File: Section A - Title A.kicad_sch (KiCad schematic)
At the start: 2 parts, among them U1 ME54BS13_V1.0

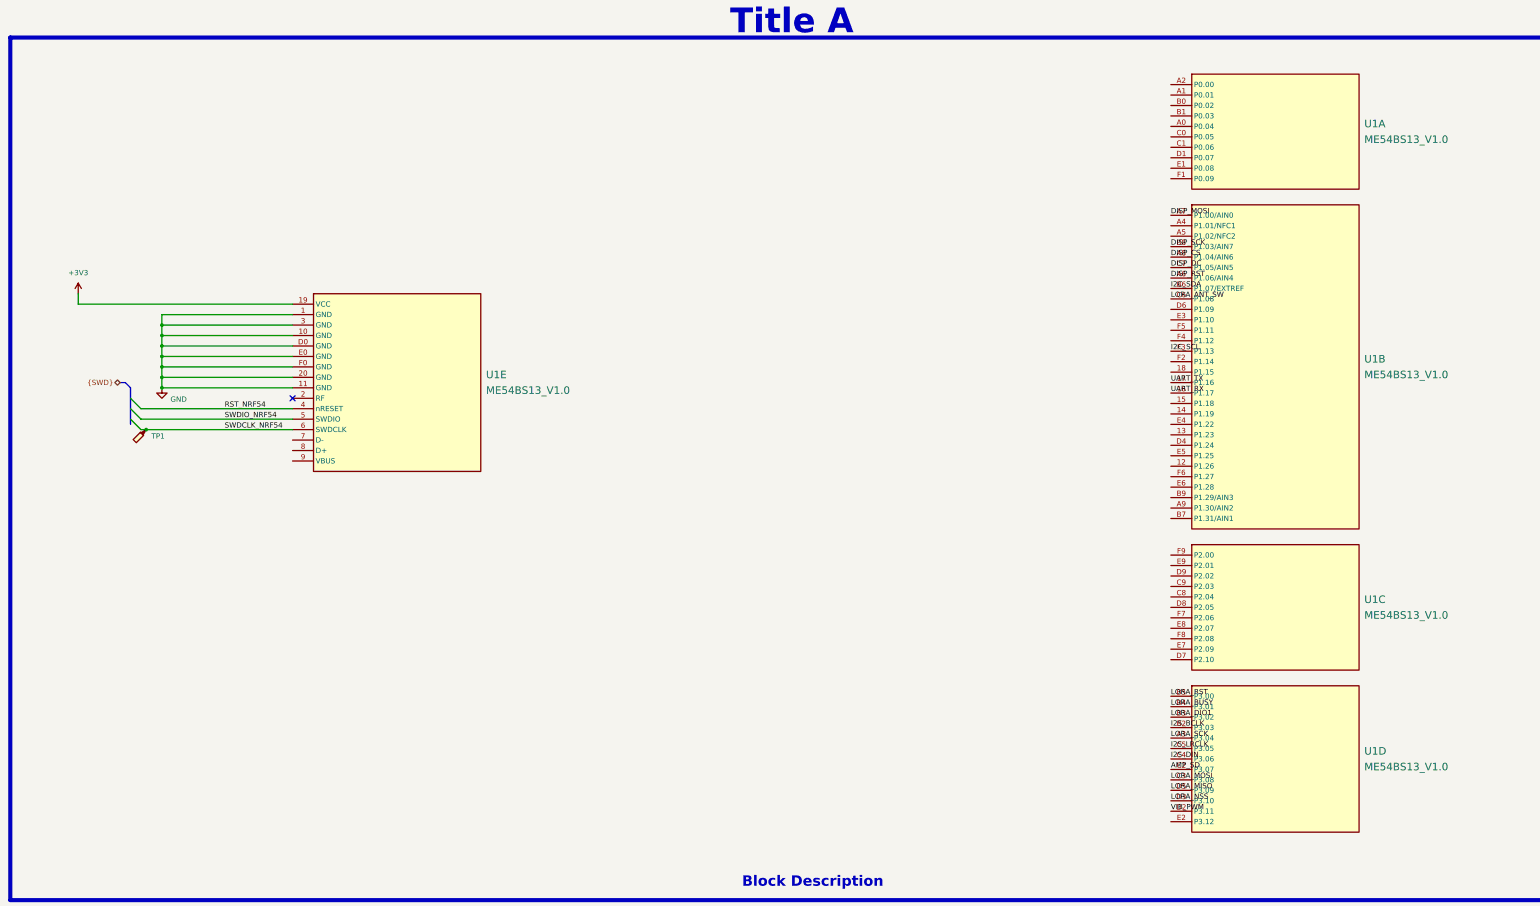
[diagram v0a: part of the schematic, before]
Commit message: Add power supply, connectors, LoRa, gas sensor, audio, and display sheets
Adds nPM1300 power management, USB-C connectors, Minew LoRa module,
multi-gas sensing (CO2/particulate), audio, and display schematics
along with the supporting component libraries and updated PCB routing.

Co-Authored-By: Claude Sonnet 5 <noreply@anthropic.com>
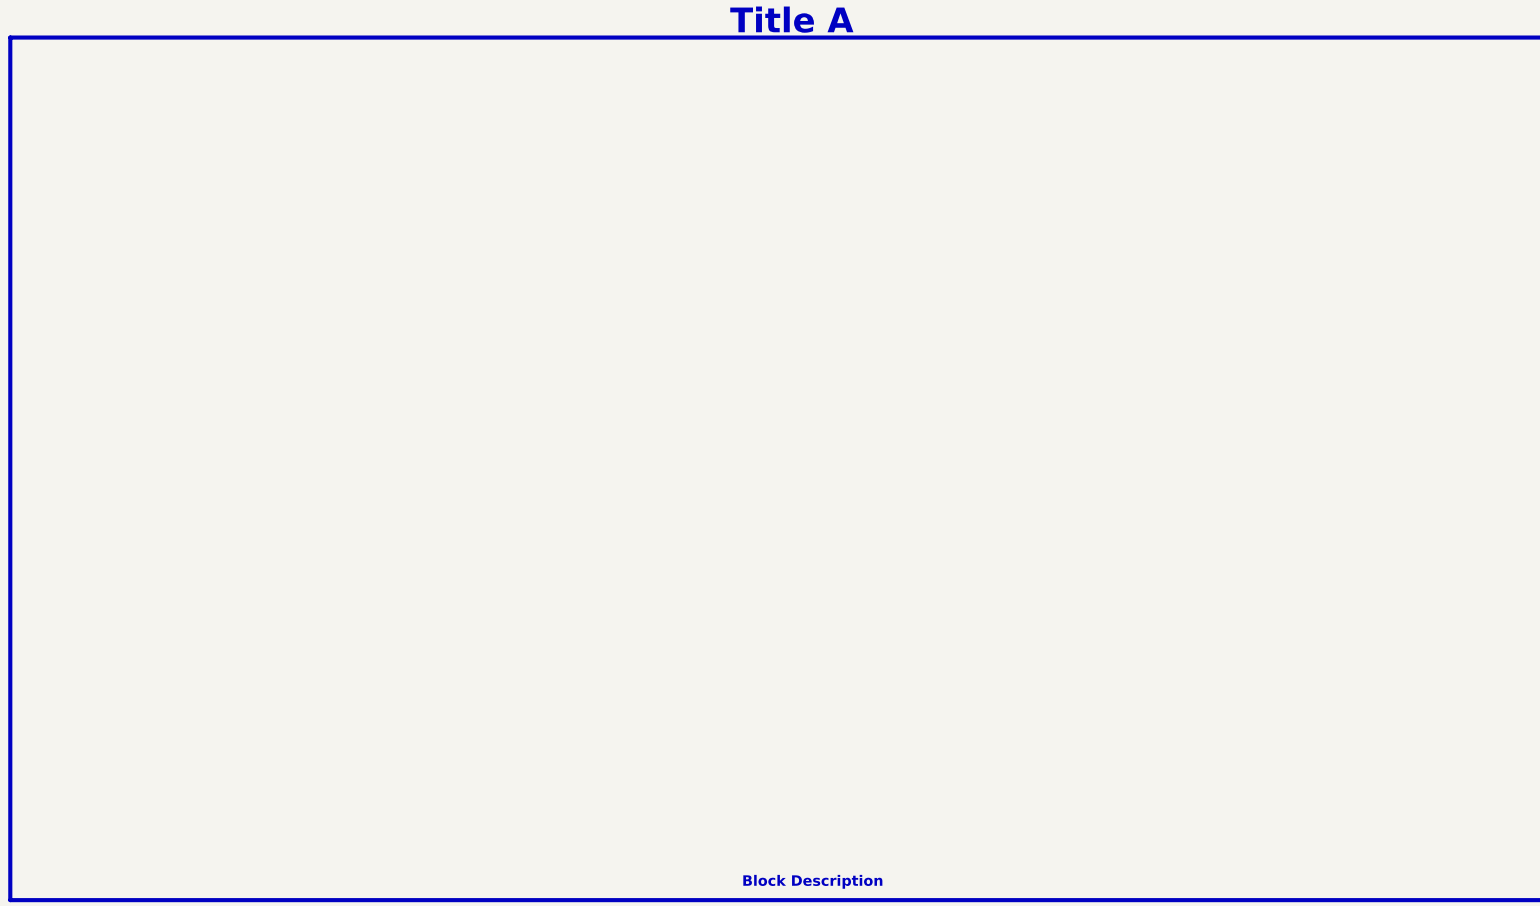
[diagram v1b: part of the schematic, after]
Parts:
- removed TP1: TestPoint_Probe, TestPoint:TestPoint_Pad_D1.0mm, symbol Connector:TestPoint_Probe
- removed U1: ME54BS13_V1.0, ME54BS13_V1.0, symbol minew:ME54BS13_V1.0
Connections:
- no-connect marks 1 -> 0
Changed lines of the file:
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@@
+(kicad_sch
+	(version 20250114)
+	(generator "eeschema")
+	(generator_version "9.0")
+	(paper "A3")
+	(title_block
+		(title "Sheet Title A")
+		(date "2025-01-12")
+		(rev "${REVISION}")
+		(company "${COMPANY}")
+	)
+	(rectangle
+		(start 15.24 30.48)
+		(end 405.13 240.03)
+		(stroke
+			(width 1)
+			(type default)
+			(color 200 200 200 1)
+		)
+		(fill
+			(type none)
+		)
+	)
+	(text "J. Pieper ADC investigation"
+		(exclude_from_sim no)
+		(at 265.938 258.318 0)
+		(effects
+			(font
+				(face "Arial")
+				(size 1.27 1.27)
+				(color 0 0 0 1)
+			)
+			(justify left bottom)
+			(href "https://jpieper.com/2023/07/24/stm32g4-adc-performance-part-2/")
+		)
+	)
+	(text "STM32G474 Datasheet p.81"
+		(exclude_from_sim no)
+		(at 265.938 254.508 0)
+		(effects
+			(font
+				(face "Arial")
+				(size 1.27 1.27)
+				(color 0 0 0 1)
+			)
+			(justify left bottom)
+			(href "https://www.st.com/resource/en/datasheet/stm32g474cb.pdf")
+		)
+	)
+	(text "AN5346"
+		(exclude_from_sim no)
+		(at 265.938 250.698 0)
+		(effects
+			(font
+				(face "Arial")
+				(size 1.27 1.27)
+				(color 0 0 0 1)
+			)
+			(justify left bottom)
+			(href "https://www.st.com/resource/en/application_note/an5346-stm32g4-adc-use-tips-and-recommendations-stmicroelectronics.pdf")
+		)
+	)
+	(text_box "[${#}] ${TITLE}"
+		(exclude_from_sim no)
+		(at 168.91 15.24 0)
+		(size 72.39 12.7)
+		(margins 4.4999 4.4999 4.4999 4.4999)
+		(stroke
+			(width -0.0001)
+			(type default)
+		)
+		(fill
+			(type none)
+		)
+		(effects
+			(font
+				(face "Times New Roman")
+				(size 6 6)
+				(thickness 1.2)
+				(bold yes)
+				(color 162 22 34 1)
+			)
+		)
+	)
+	(text_box "Block Description"
+		(exclude_from_sim no)
+		(at 16.51 231.14 0)
+		(size 387.35 7.62)
+		(margins 1.9049 1.9049 1.9049 1.9049)
+		(stroke
+			(width -0.0001)
+			(type default)
+		)
+		(fill
+			(type none)
+		)
+		(effects
+			(font
+				(face "Times New Roman")
+				(size 2.54 2.54)
+				(thickness 0.508)
+				(bold yes)
+				(color 162 22 34 1)
+			)
+			(justify bottom)
+		)
+	)
+)
